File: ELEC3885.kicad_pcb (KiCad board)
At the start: 2 copper layers, 138 x 81.5 mm, 41 parts, among them J1 MicInstIn, J2 LineIn, J3 HeadPhoneOut, J4 LineOutR, J5 LineOutL, J6 Conn_01x24_Female, J7 Conn_01x24_Female, J8 Conn_01x06_Female, J9 Conn_01x05_Female, SW1 SW_Push, SW2 SW_Push, SW3 SW_Push, SW4 SW_Push, U1 AP7313, U2 SGTL5000XNLA3, U3 Teensy4.1

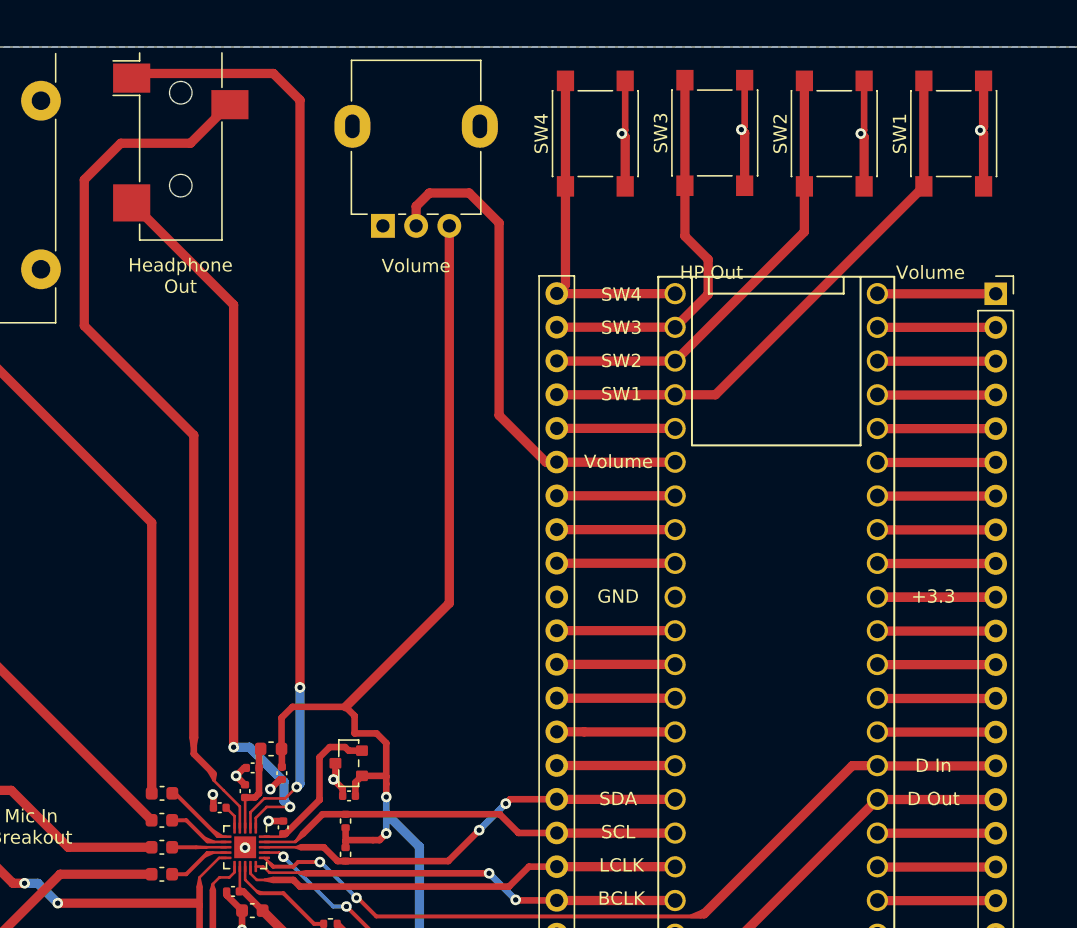
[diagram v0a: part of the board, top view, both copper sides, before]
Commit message: Moved to Rev 3, button + LED ui added
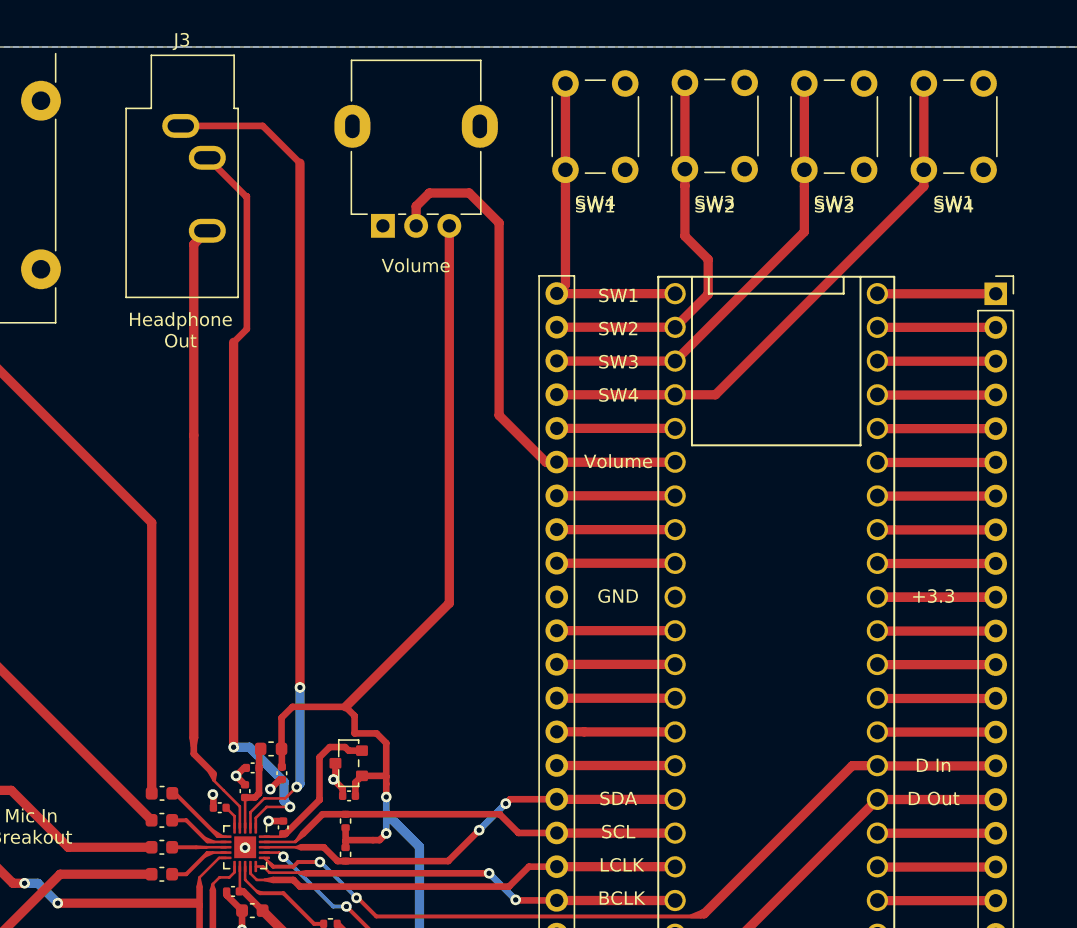
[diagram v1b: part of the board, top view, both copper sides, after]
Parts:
- J3: footprint Connector_Audio:Jack_3.5mm_CUI_SJ-3523-SMT_Horizontal -> Connector_Audio:Jack_3.5mm_CUI_SJ1-3533NG_Horizontal
- SW1, SW2, SW3: footprint Button_Switch_SMD:SW_Push_1P1T_NO_6x6mm_H9.5mm -> Button_Switch_THT:SW_PUSH_6mm
- SW4: footprint Button_Switch_SMD:SW_Push_1P1T_NO_6x6mm_H9.5mm -> Button_Switch_THT:SW_PUSH_6mm_H4.3mm
- moved SW3 3.53 mm to (170.5, 74.2)
- moved SW1 3.53 mm to (188.5, 74.2)
- moved SW2 3.53 mm to (179.5, 74.2)
- moved SW4 3.53 mm to (161.5, 74.2)
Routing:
- net GND: track 46.3 -> 12.6 mm, vias 12 -> 8
- net /Audio/HP_L: track 88.5 -> 68.4 mm
- net /Audio/HP_VGND: track 71.7 -> 62.7 mm
- net /Audio/HP_R: track 54.8 -> 56.7 mm
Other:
- board text removed: "HP Out"

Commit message: Rev3 PCB layout started
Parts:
- removed J8: Conn_01x06_Female, Connector_PinSocket_2.54mm:PinSocket_1x06_P2.54mm_Vertical
- removed MK1: InternalMic, Connector_PinSocket_2.54mm:PinSocket_1x02_P2.54mm_Vertical
- removed SW1, SW2, SW3: SW_Push, Button_Switch_THT:SW_PUSH_6mm
- removed SW4: SW_Push, Button_Switch_THT:SW_PUSH_6mm_H4.3mm
- added C13: 4u7, Capacitor_SMD:C_0402_1005Metric, F.Cu at (250.7, 72.8)
- added C14: 4u7, Capacitor_SMD:C_0402_1005Metric, F.Cu at (249.8, 76.0)
- added C15: 100n, Capacitor_SMD:C_0402_1005Metric, B.Cu at (115.2, 84.5)
- added C16: 6n8, Capacitor_SMD:C_0402_1005Metric, B.Cu at (103.7, 79.4)
- added C17: 6n8, Capacitor_SMD:C_0402_1005Metric, B.Cu at (101.2, 79.4)
- added C18: 8u2, Capacitor_SMD:C_0402_1005Metric, B.Cu at (106.8, 86.4)
- added C19: 22u, Capacitor_SMD:C_0603_1608Metric, F.Cu at (250.1, 78.3)
- added C20: 22u, Capacitor_SMD:C_0603_1608Metric, F.Cu at (252.2, 89.9)
- added D1: LED_RGBK, LED_THT:LED_D5.0mm-4_RGB, F.Cu at (106.0, 140.4)
- added D10: LED, LED_SMD:LED_0201_0603Metric, F.Cu at (258.7, 68.0)
- added D2: LED_RGBK, LED_THT:LED_D5.0mm-4_RGB, F.Cu at (122.8, 140.4)
- added D3: LED_RGBK, LED_THT:LED_D5.0mm-4_RGB, F.Cu at (139.5, 140.4)
- added D4: LED_RGBK, LED_THT:LED_D5.0mm-4_RGB, F.Cu at (156.3, 140.4)
- added D5: LED_RGBK, LED_THT:LED_D5.0mm-4_RGB, F.Cu at (173.0, 140.4)
- added D6: LED_RGBK, LED_THT:LED_D5.0mm-4_RGB, F.Cu at (189.8, 140.4)
- added D7: LED_RGBK, LED_THT:LED_D5.0mm-4_RGB, F.Cu at (206.5, 140.4)
- added D8: LED_RGBK, LED_THT:LED_D5.0mm-4_RGB, F.Cu at (223.3, 140.4)
- added L1: 22uH, Inductor_SMD:L_6.3x6.3_H3, F.Cu at (255.9, 82.9)
- added R10: 100R, Resistor_SMD:R_0402_1005Metric, F.Cu at (198.5, 148.8)
- added R11: 100R, Resistor_SMD:R_0402_1005Metric, F.Cu at (215.2, 148.8)
- added R12: 100R, Resistor_SMD:R_0402_1005Metric, F.Cu at (84.2, 122.6)
- added R13: 100R, Resistor_SMD:R_0402_1005Metric, F.Cu at (82.2, 125.2)
- added R14: 270R, Resistor_SMD:R_0402_1005Metric, F.Cu at (218.2, 140.4)
- added R15: 270R, Resistor_SMD:R_0402_1005Metric, F.Cu at (218.2, 139.1)
- added R16: 270R, Resistor_SMD:R_0402_1005Metric, F.Cu at (218.2, 137.9)
- added R17: 270R, Resistor_SMD:R_0402_1005Metric, F.Cu at (184.7, 140.4)
- added R18: 270R, Resistor_SMD:R_0402_1005Metric, F.Cu at (184.7, 139.1)
- added R19: 270R, Resistor_SMD:R_0402_1005Metric, F.Cu at (184.7, 137.9)
- added R20: 270R, Resistor_SMD:R_0402_1005Metric, F.Cu at (201.4, 140.4)
- added R21: 270R, Resistor_SMD:R_0402_1005Metric, F.Cu at (201.4, 139.1)
- added R22: 270R, Resistor_SMD:R_0402_1005Metric, F.Cu at (151.2, 137.9)
- added R23: 270R, Resistor_SMD:R_0402_1005Metric, F.Cu at (151.2, 140.5)
- added R24: 270R, Resistor_SMD:R_0402_1005Metric, F.Cu at (167.9, 139.1)
- added R25: 270R, Resistor_SMD:R_0402_1005Metric, F.Cu at (201.4, 137.8)
- added R26: 270R, Resistor_SMD:R_0402_1005Metric, F.Cu at (134.4, 140.4)
- added R27: 270R, Resistor_SMD:R_0402_1005Metric, F.Cu at (151.2, 139.2)
- added R28: 270R, Resistor_SMD:R_0402_1005Metric, F.Cu at (167.9, 137.8)
- added R29: 270R, Resistor_SMD:R_0402_1005Metric, F.Cu at (167.9, 140.4)
- added R30: 270R, Resistor_SMD:R_0402_1005Metric, F.Cu at (100.9, 139.1)
- added R31: 270R, Resistor_SMD:R_0402_1005Metric, F.Cu at (117.7, 137.9)
- added R32: 270R, Resistor_SMD:R_0402_1005Metric, F.Cu at (117.7, 140.5)
- added R33: 270R, Resistor_SMD:R_0402_1005Metric, F.Cu at (134.4, 139.1)
- added R34: 270R, Resistor_SMD:R_0402_1005Metric, F.Cu at (100.9, 137.9)
- added R35: 270R, Resistor_SMD:R_0402_1005Metric, F.Cu at (100.9, 140.4)
- added R36: 270R, Resistor_SMD:R_0402_1005Metric, F.Cu at (117.7, 139.2)
- added R37: 270R, Resistor_SMD:R_0402_1005Metric, F.Cu at (134.4, 137.8)
- added R38: 1k, Resistor_SMD:R_0402_1005Metric, B.Cu at (99.2, 79.4)
- added R39: 1k, Resistor_SMD:R_0402_1005Metric, B.Cu at (105.7, 79.4)
- added R4: 2k, Resistor_SMD:R_0402_1005Metric, F.Cu at (247.9, 70.5)
- added R40: 100k, Resistor_SMD:R_0603_1608Metric, B.Cu at (96.8, 85.7)
- added R41: 100k, Resistor_SMD:R_0603_1608Metric, B.Cu at (96.8, 84.0)
- added R42: 9k, Resistor_SMD:R_0603_1608Metric, B.Cu at (99.7, 81.6)
- added R43: 9k, Resistor_SMD:R_0603_1608Metric, B.Cu at (105.0, 81.0)
- added R44: 10k, Resistor_SMD:R_0603_1608Metric, B.Cu at (104.7, 82.6)
- added R45: 10k, Resistor_SMD:R_0603_1608Metric, B.Cu at (105.5, 85.0)
- added R46: 1k, Resistor_SMD:R_0402_1005Metric, B.Cu at (106.8, 87.8)
- added R47: 100R, Resistor_SMD:R_0402_1005Metric, B.Cu at (108.9, 86.4)
- added R48: R, Resistor_SMD:R_0402_1005Metric, F.Cu at (251.9, 70.6)
- added R49: 15k, Resistor_SMD:R_0603_1608Metric, F.Cu at (251.4, 86.0)
- added R5: 100R, Resistor_SMD:R_0402_1005Metric, F.Cu at (114.7, 148.8)
- added R50: 2k, Resistor_SMD:R_0402_1005Metric, F.Cu at (250.0, 85.6)
- added R6: 100R, Resistor_SMD:R_0402_1005Metric, F.Cu at (131.5, 148.8)
- added R7: 100R, Resistor_SMD:R_0402_1005Metric, F.Cu at (148.2, 148.8)
- added R8: 100R, Resistor_SMD:R_0402_1005Metric, F.Cu at (165.2, 148.8)
- added R9: 100R, Resistor_SMD:R_0402_1005Metric, F.Cu at (181.7, 148.8)
- added SW10: SW_Push, Button_Switch_SMD:SW_Push_1P1T_NO_6x6mm_H9.5mm, F.Cu at (189.8, 149.8)
- added SW11: SW_Push, Button_Switch_SMD:SW_Push_1P1T_NO_6x6mm_H9.5mm, F.Cu at (206.5, 149.8)
- added SW12: SW_Push, Button_Switch_SMD:SW_Push_1P1T_NO_6x6mm_H9.5mm, F.Cu at (223.2, 149.8)
- added SW5: SW_Push, Button_Switch_SMD:SW_Push_1P1T_NO_6x6mm_H9.5mm, F.Cu at (106.0, 149.8)
- added SW6: SW_Push, Button_Switch_SMD:SW_Push_1P1T_NO_6x6mm_H9.5mm, F.Cu at (122.8, 149.8)
- added SW7: SW_Push, Button_Switch_SMD:SW_Push_1P1T_NO_6x6mm_H9.5mm, F.Cu at (139.5, 149.8)
- added SW8: SW_Push, Button_Switch_SMD:SW_Push_1P1T_NO_6x6mm_H9.5mm, F.Cu at (156.3, 149.8)
- added SW9: SW_Push, Button_Switch_SMD:SW_Push_1P1T_NO_6x6mm_H9.5mm, F.Cu at (173.0, 149.8)
- added TP1: TP_RCLK, TestPoint:TestPoint_Pad_D1.0mm, F.Cu at (14.9, 83.5)
- added TP2: TP_SRCLK_N, TestPoint:TestPoint_Pad_D1.0mm, F.Cu at (14.9, 86.6)
- added TP3: TP_SRCLK, TestPoint:TestPoint_Pad_D1.0mm, F.Cu at (14.9, 89.7)
- added TP4: TP_DS, TestPoint:TestPoint_Pad_D1.0mm, F.Cu at (14.9, 92.7)
- added TP5: TP_BUTTON_ARRAY, TestPoint:TestPoint_Pad_D1.0mm, F.Cu at (14.9, 95.8)
- added U10: MT3608, Package_TO_SOT_SMD:SOT-23-6, F.Cu at (250.3, 81.2)
- added U11: L7805, Package_TO_SOT_SMD:TO-252-2, F.Cu at (254.4, 94.8)
- added U4: 74HC595, Package_SO:SOP-16_4.4x10.4mm_P1.27mm, F.Cu at (155.0, 128.9)
- added U5: 74HC595, Package_SO:SOP-16_4.4x10.4mm_P1.27mm, F.Cu at (187.8, 128.9)
- added U6: 74HC595, Package_SO:SOP-16_4.4x10.4mm_P1.27mm, F.Cu at (105.2, 128.9)
- added U7: LCD_Conn, Connector_PinHeader_2.54mm:PinHeader_1x08_P2.54mm_Vertical, F.Cu at (-20.8, 114.4)
- added U8: NE5532, Package_SO:SOIC-8-1EP_3.9x4.9mm_P1.27mm_EP2.29x3mm, B.Cu at (110.8, 83.1)
- added U9: MCP73831-2-OT, Package_TO_SOT_SMD:SOT-23-5, F.Cu at (248.3, 73.4)
- C1, C10, C11, C12, C13, C14, C2, C3, C4, C5, C6, C7, C9, J1, J2, J4, J5, R1, R2, R3, R4, U1, U2, U3: moved to B.Cu
- C8: value .1uF -> 0.1uF; moved to B.Cu
- FB1: value FerriteBead -> 600; moved to B.Cu
- J3: footprint Connector_Audio:Jack_3.5mm_CUI_SJ1-3533NG_Horizontal -> Connector_Audio:Jack_3.5mm_CUI_SJ-3523-SMT_Horizontal; moved to B.Cu
- J6: value Conn_01x24_Female -> Conn_LiPo; footprint Connector_PinSocket_2.54mm:PinSocket_1x24_P2.54mm_Vertical -> Connector_JST:JST_EH_S2B-EH_1x02_P2.50mm_Horizontal; moved to B.Cu
- J7: value Conn_01x24_Female -> USB_B_Micro; footprint Connector_PinSocket_2.54mm:PinSocket_1x24_P2.54mm_Vertical -> Connector_USB:USB_Micro-B_Amphenol_10103594-0001LF_Horizontal; moved to B.Cu
- moved C14 253.2 mm to (376.8, 64.3), turned to 0 degrees
- moved R4 251.0 mm to (376.8, 66.1), turned to 0 degrees
- moved C13 246.3 mm to (376.3, 69.4), turned to -90 degrees
- moved C5 244.7 mm to (366.6, 61.0), turned to -90 degrees
- moved C4 242.2 mm to (364.6, 61.0), turned to -90 degrees
- moved C12 239.7 mm to (362.5, 61.0), turned to 90 degrees
- moved C2 239.7 mm to (367.9, 66.3), turned to 90 degrees
- moved C1 239.7 mm to (369.4, 67.8), turned to 90 degrees
- moved C11 237.2 mm to (360.5, 61.0), turned to 90 degrees
- moved U2 234.5 mm to (364.6, 67.3), turned to 0 degrees
- moved R1 233.7 mm to (370.4, 73.7), turned to 90 degrees
- moved C6 233.2 mm to (361.6, 65.3), turned to -90 degrees
- moved C9 229.4 mm to (360.4, 67.3), turned to 180 degrees
- moved C8 229.2 mm to (363.1, 70.1), turned to 180 degrees
- moved C10 226.6 mm to (358.6, 67.8), turned to 90 degrees
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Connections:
- J1 pad 3: GND -> /Audio/MIC_VGND
- J6 pad 1: Net-(J6-Pad1) -> Net-(J6-Pin_1)
- J6 pad 2: Net-(J6-Pad2) -> GND
- J7 pad 1: Net-(J7-Pad1) -> Net-(D9-K)
- J7 pad 2: GND -> unconnected-(J7-D--Pad2)
- J7 pad 3: +3.3V -> unconnected-(J7-D+-Pad3)
- J7 pad 4: /Audio/MCLK -> unconnected-(J7-ID-Pad4)
- J7 pad 5: Net-(J7-Pad5) -> GND
- J7 pad 6: /Audio/BCLK -> GND
- U3 pad 11: Net-(J6-Pad14) -> /Teensy/LCD_DC
- U3 pad 12: Net-(J6-Pad13) -> /Teensy/LCD_CS
- U3 pad 13: Net-(J6-Pad12) -> /Teensy/LCD_MOSI
- U3 pad 14: Net-(J6-Pad11) -> /Teensy/LCD_MISO
- U3 pad 16: Net-(J6-Pad9) -> unconnected-(U3-24_A10_TX6_SCL2-Pad16)
- U3 pad 17: Net-(J6-Pad8) -> unconnected-(U3-25_A11_RX6_SDA2-Pad17)
- U3 pad 18: Net-(J6-Pad7) -> unconnected-(U3-26_A12_MOSI1-Pad18)
- U3 pad 19: Net-(J6-Pad6) -> unconnected-(U3-27_A13_SCK1-Pad19)
- U3 pad 2: Net-(J6-Pad23) -> unconnected-(U3-0_RX1_CRX2_CS1-Pad2)
- U3 pad 20: Net-(J6-Pad5) -> unconnected-(U3-28_RX7-Pad20)
- U3 pad 21: Net-(J6-Pad4) -> unconnected-(U3-29_TX7-Pad21)
- U3 pad 22: Net-(J6-Pad3) -> unconnected-(U3-30_CRX3-Pad22)
- U3 pad 23: Net-(J6-Pad2) -> unconnected-(U3-31_CTX3-Pad23)
- U3 pad 24: Net-(J6-Pad1) -> unconnected-(U3-32_OUT1B-Pad24)
- U3 pad 25: /Teensy/BUTTON_3 -> unconnected-(U3-33_MCLK2-Pad25)
- U3 pad 26: /Teensy/BUTTON_2 -> unconnected-(U3-34_RX8-Pad26)
- U3 pad 27: /Teensy/BUTTON_1 -> unconnected-(U3-35_TX8-Pad27)
- U3 pad 28: /Teensy/BUTTON_0 -> unconnected-(U3-36_CS-Pad28)
- U3 pad 29: Net-(J7-Pad20) -> unconnected-(U3-37_CS-Pad29)
- U3 pad 3: Net-(J6-Pad22) -> unconnected-(U3-1_TX1_CTX2_MISO1-Pad3)
- U3 pad 31: Net-(J7-Pad18) -> unconnected-(U3-39_MISO1_OUT1A-Pad31)
- U3 pad 32: Net-(J7-Pad17) -> unconnected-(U3-40_A16-Pad32)
- U3 pad 33: Net-(J7-Pad16) -> /Teensy/BUTTON_ARRAY
- U3 pad 35: Net-(J7-Pad14) -> /Teensy/LCD_CLK
- U3 pad 36: Net-(J7-Pad13) -> unconnected-(U3-14_A0_TX3_SPDIF_OUT-Pad36)
- U3 pad 37: Net-(J7-Pad12) -> unconnected-(U3-15_A1_RX3_SPDIF_IN-Pad37)
- U3 pad 38: Net-(J7-Pad11) -> unconnected-(U3-16_A2_RX4_SCL1-Pad38)
- U3 pad 39: Net-(J7-Pad10) -> unconnected-(U3-17_A3_TX4_SDA1-Pad39)
- U3 pad 4: Net-(J6-Pad21) -> unconnected-(U3-2_OUT2-Pad4)
- U3 pad 44: Net-(J7-Pad5) -> unconnected-(U3-22_A8_CTX1-Pad44)
- U3 pad 48: Net-(J7-Pad1) -> unconnected-(U3-VIN-Pad48)
- U3 pad 5: Net-(J6-Pad20) -> unconnected-(U3-3_LRCLK2-Pad5)
- U3 pad 6: Net-(J6-Pad19) -> unconnected-(U3-4_BCLK2-Pad6)
- U3 pad 7: Net-(J6-Pad18) -> unconnected-(U3-5_IN2-Pad7)
- U3 pad 8: Net-(J6-Pad17) -> unconnected-(U3-6_OUT1D-Pad8)
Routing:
- net +3.3V: track 223.5 -> 82.7 mm, vias 4 -> 3
- net /Teensy/BUTTON_ARRAY: track 0.00 -> 128.6 mm
- net /UI/LED_SRCLK: track 0.00 -> 91.7 mm
- net /UI/LED_RCLK: track 0.00 -> 89.8 mm, vias 0 -> 4
- net Net-(U4-~{OE}): track 0.00 -> 87.5 mm, vias 0 -> 4
- net /Audio/LINE_OUT_R: track 78.4 -> 0.00 mm
- net /Audio/LINE_IN_R: track 67.8 -> 0.00 mm
- net /Audio/HP_L: track 68.4 -> 8.27 mm
- net Net-(U4-QH'): track 0.00 -> 59.1 mm, vias 0 -> 2
- net /Audio/LINE_IN_L: track 54.2 -> 0.00 mm
- net /Audio/LINE_OUT_L: track 51.7 -> 0.00 mm
- net /Audio/D_IN: track 62.0 -> 10.6 mm
- net /Audio/D_OUT: track 62.5 -> 12.3 mm
- net /Audio/HP_VGND: track 62.7 -> 13.1 mm
- net /Audio/HP_R: track 56.7 -> 10.6 mm
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- added copper zone on In1.Cu, net GND
- removed copper zone on B.Cu, net GND
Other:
- board size 138 x 81.5 mm -> 175 x 102 mm
- copper layers 2 -> 4
- board text removed: "+"
- board text removed: "+3.3"
- board text removed: "-"
- board text removed: "BCLK"
- board text removed: "D In"
- board text removed: "D Out"
- board text removed: "ECM"
- board text removed: "Headphone Out"
- board text removed: "In"
- board text removed: "LCLK"
- board text removed: "Line In"
- board text removed: "Line Out L"
- board text removed: "Line Out R"
- board text removed: "MCLK"
- board text removed: "Mic In"
- board text removed: "Mic In Breakout"
- board text removed: "SCL"
- board text removed: "SDA"
- board text removed: "SW1"
- board text removed: "SW2"
- board text removed: "SW3"
- board text removed: "SW4"
- board text removed: "Volume"

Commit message: Rev3 rework, diff amp jumpers added
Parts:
- removed the C13 at (376.3, 69.4)
- removed the C14 at (376.8, 64.3)
- removed the R4 at (376.8, 66.1)
- added D11: SS34, Diode_SMD:D_SMC, F.Cu at (230.8, 66.0)
- added D9: uClamp0571P, Luke_library:DFN1610-2, F.Cu at (235.1, 40.4)
- added JP1: JP1, Jumper:SolderJumper-3_P1.3mm_Open_RoundedPad1.0x1.5mm, B.Cu at (85.1, 43.5)
- added JP2: JP2, Jumper:SolderJumper-3_P1.3mm_Open_RoundedPad1.0x1.5mm, B.Cu at (75.3, 43.5)
- added JP3: JP3, Jumper:SolderJumper-3_P1.3mm_Open_RoundedPad1.0x1.5mm, B.Cu at (80.2, 43.5)
- added RV2: 10k, Potentiometer_THT:Potentiometer_Alpha_RD901F-40-00D_Single_Vertical, F.Cu at (166.1, 69.1)
- added RV3: 10k, Potentiometer_THT:Potentiometer_Alpha_RD901F-40-00D_Single_Vertical, F.Cu at (188.0, 69.1)
- added RV4: 10k, Potentiometer_THT:Potentiometer_Alpha_RD901F-40-00D_Single_Vertical, F.Cu at (209.9, 69.1)
- added SW1: SW_SPST, Button_Switch_THT:SW_CuK_OS102011MA1QN1_SPDT_Angled, F.Cu at (239.6, 52.5)
- U7: footprint Connector_PinHeader_2.54mm:PinHeader_1x08_P2.54mm_Vertical -> Luke_library:Adafruit_3.5_TFT_SPI
- moved C5 241.4 mm to (126.3, 83.1), turned to 0 degrees
- moved C4 239.5 mm to (126.3, 85.1), turned to 0 degrees
- moved C12 237.7 mm to (126.3, 87.2), turned to 180 degrees
- moved C2 236.8 mm to (131.6, 81.8), turned to 180 degrees
- moved C1 236.6 mm to (133.1, 80.4), turned to 180 degrees
- moved C11 235.9 mm to (126.3, 89.2), turned to 180 degrees
- moved U2 232.7 mm to (132.5, 85.1), turned to 90 degrees
- moved C6 232.1 mm to (130.6, 88.1), turned to 0 degrees
- moved R1 231.5 mm to (139.0, 79.4), turned to 180 degrees
- moved C9 228.9 mm to (132.5, 89.4), turned to -90 degrees
- moved C8 228.3 mm to (135.4, 86.6), turned to -90 degrees
- moved C10 226.7 mm to (133.1, 91.1), turned to 180 degrees
- moved R3 225.2 mm to (140.1, 84.6), turned to -90 degrees
- moved C7 224.7 mm to (135.3, 90.7), turned to 90 degrees
- moved FB1 223.9 mm to (134.5, 92.5), turned to 180 degrees
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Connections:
- C19 pad 1: Net-(J6-Pin_1) -> Net-(SW1-B)
- J1 pad 1: Net-(J1-Pad1) -> Net-(JP1-C)
- J1 pad 2: Net-(J1-Pad2) -> Net-(JP2-C)
- J1 pad 3: /Audio/MIC_VGND -> Net-(JP3-C)
- L1 pad 1: Net-(J6-Pin_1) -> Net-(SW1-B)
- R17 pad 2: Net-(D6-RA) -> Net-(D7-RA)
- R18 pad 2: Net-(D6-GA) -> Net-(D7-GA)
- R19 pad 2: Net-(D6-BA) -> Net-(D7-BA)
- R20 pad 2: Net-(D7-RA) -> Net-(D6-RA)
- R21 pad 2: Net-(D7-GA) -> Net-(D6-GA)
- R25 pad 2: Net-(D7-BA) -> Net-(D6-BA)
- R38 pad 1: Net-(J1-Pad2) -> Net-(JP2-B)
- R39 pad 1: Net-(J1-Pad1) -> Net-(JP1-A)
- TP1 pad 1: /UI/LED_RCLK -> /Teensy/LED_RCLK
- TP3 pad 1: /UI/LED_SRCLK -> /Teensy/LED_SRCLK
- TP4 pad 1: /UI/LED_DS -> /Teensy/LED_DS
- U10 pad 4: Net-(J6-Pin_1) -> Net-(SW1-B)
- U10 pad 5: Net-(J6-Pin_1) -> Net-(SW1-B)
- U3 pad 16: unconnected-(U3-24_A10_TX6_SCL2-Pad16) -> /Teensy/UI_POT1
- U3 pad 17: unconnected-(U3-25_A11_RX6_SDA2-Pad17) -> /Teensy/UI_POT2
- U3 pad 18: unconnected-(U3-26_A12_MOSI1-Pad18) -> /Teensy/UI_POT3
- U3 pad 19: unconnected-(U3-27_A13_SCK1-Pad19) -> /Audio/VOLUME_CONTROL
- U3 pad 30: /Audio/VOLUME_CONTROL -> unconnected-(U3-38_CS1_IN1-Pad30)
- U3 pad 37: unconnected-(U3-15_A1_RX3_SPDIF_IN-Pad37) -> /Teensy/LED_SRCLK
- U3 pad 38: unconnected-(U3-16_A2_RX4_SCL1-Pad38) -> /Teensy/LED_RCLK
- U3 pad 39: unconnected-(U3-17_A3_TX4_SDA1-Pad39) -> /Teensy/LED_DS
- U3 pad 48: unconnected-(U3-VIN-Pad48) -> +5V
- U4 pad 11: /UI/LED_SRCLK -> /Teensy/LED_SRCLK
- U4 pad 12: /UI/LED_RCLK -> /Teensy/LED_RCLK
- U5 pad 11: /UI/LED_SRCLK -> /Teensy/LED_SRCLK
- U5 pad 12: /UI/LED_RCLK -> /Teensy/LED_RCLK
- U5 pad 14: /UI/LED_DS -> /Teensy/LED_DS
- U6 pad 11: /UI/LED_SRCLK -> /Teensy/LED_SRCLK
- U6 pad 12: /UI/LED_RCLK -> /Teensy/LED_RCLK
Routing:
- net +5V: track 1.94 -> 235.8 mm, vias 0 -> 6
- net /Teensy/BUTTON_ARRAY: track 128.6 -> 0.00 mm
- net /Audio/HP_L: track 8.27 -> 130.2 mm, vias 0 -> 2
- net /Teensy/LED_SRCLK: track 0.00 -> 118.2 mm, vias 0 -> 2
- net /Audio/LINE_OUT_R: track 0.00 -> 114.0 mm, vias 0 -> 2
- net /Teensy/LED_RCLK: track 0.00 -> 112.8 mm, vias 0 -> 8
- net +3.3V: track 82.7 -> 192.8 mm, vias 3 -> 7
- net /Audio/HP_VGND: track 13.1 -> 121.6 mm, vias 2 -> 0
- net /Audio/MEMS_IN: track 0.00 -> 105.2 mm, vias 0 -> 3
- net /Audio/HP_R: track 10.6 -> 115.5 mm, vias 2 -> 0
- net /Audio/LINE_OUT_L: track 0.00 -> 94.3 mm, vias 0 -> 2
- net /UI/LED_SRCLK: track 91.7 -> 0.00 mm
- net /UI/LED_RCLK: track 89.8 -> 0.00 mm, vias 4 -> 0
- net /Audio/LINE_IN_R: track 0.00 -> 79.3 mm
- net /Audio/MIC_IN: track 12.5 -> 85.2 mm, vias 0 -> 4
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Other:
- board size 175 x 102 mm -> 190 x 130 mm
- board text added: "DA"
- board text added: "HEADPHONE"
- board text added: "INTERNAL MIC"
- board text added: "LCD"
- board text added: "LINE IN"
- board text added: "LINE OUT"
- board text added: "MIC IN"
- board text added: "N"
- board text added: "SD CARD SLOT"
- board text added: "USB PWR"
- board text removed: "+3.3V"
- board text removed: "GND"
- board text removed: "MEMS Breakout"
- board text removed: "MEMS In"

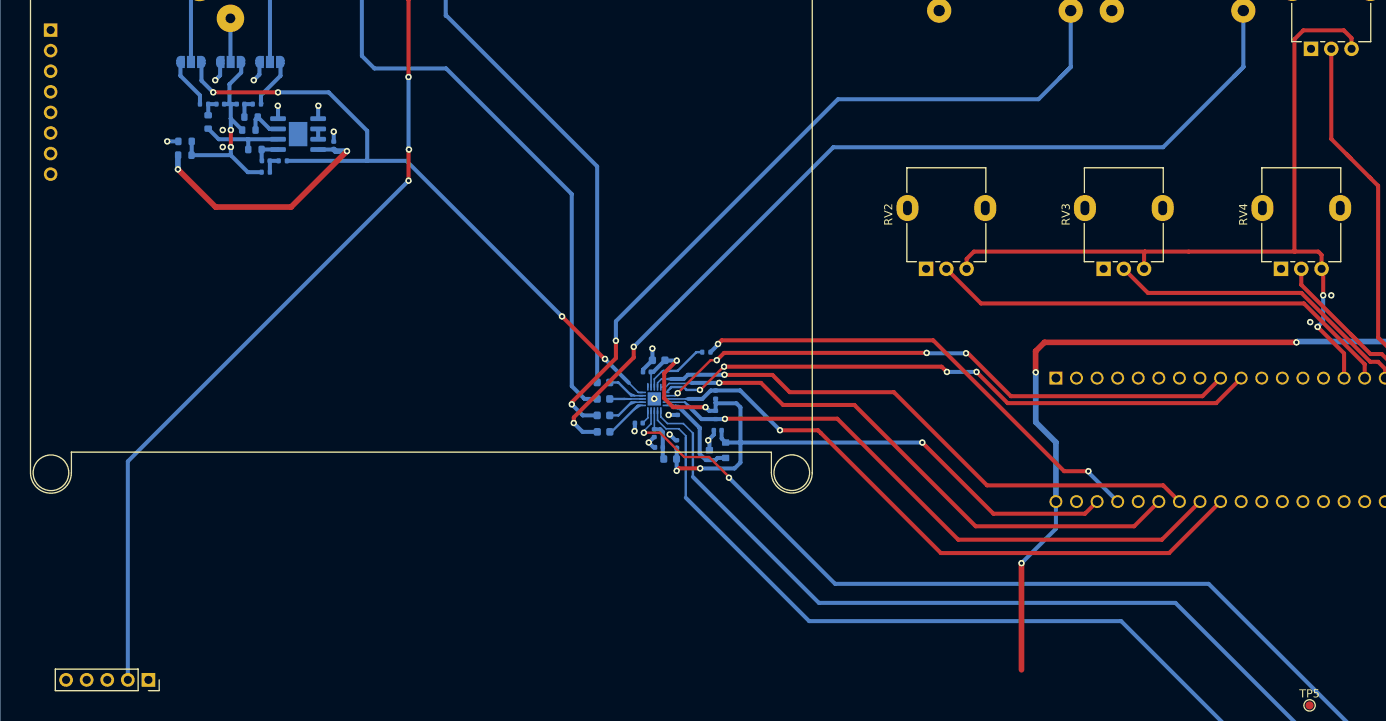
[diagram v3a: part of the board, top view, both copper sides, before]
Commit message: LCD footprint fix
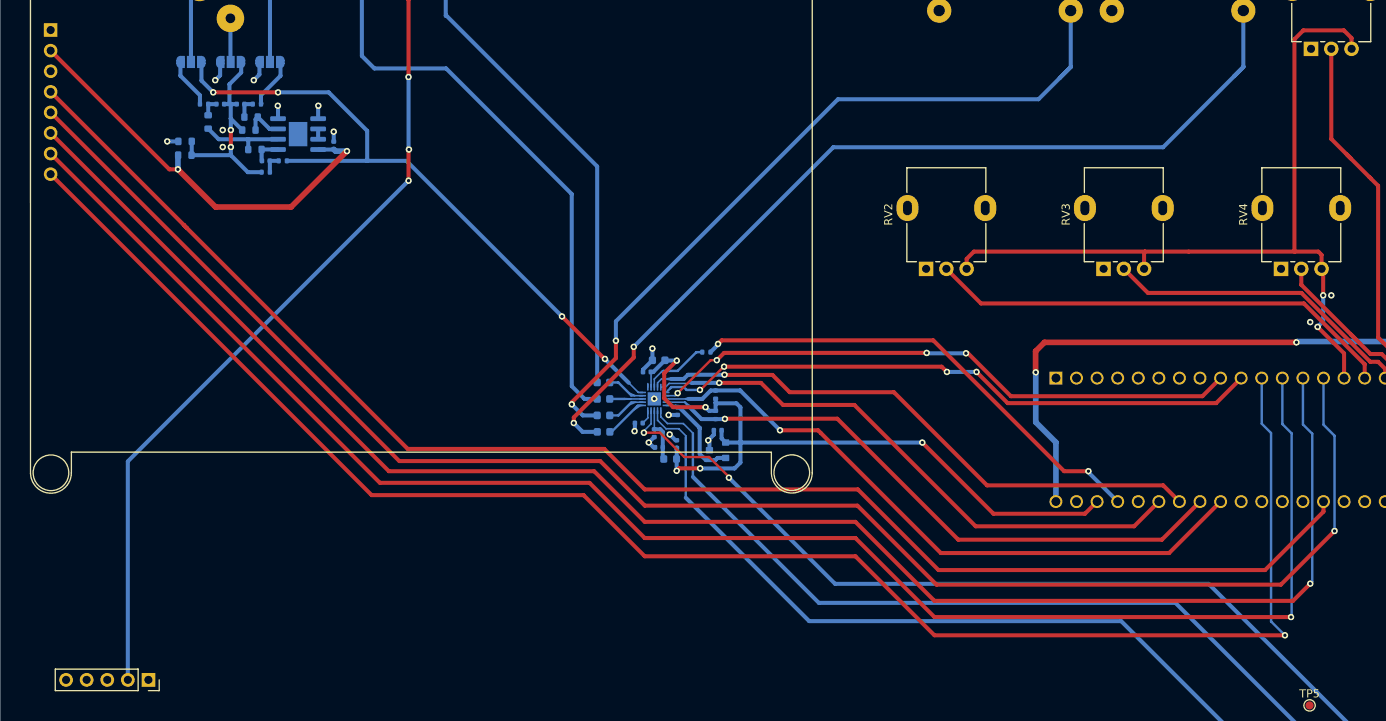
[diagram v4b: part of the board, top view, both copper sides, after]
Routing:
- net /Teensy/LCD_DC: track 0.00 -> 208.8 mm, vias 0 -> 1
- net /Teensy/LCD_CS: track 0.00 -> 206.8 mm, vias 0 -> 1
- net /Teensy/LCD_MOSI: track 0.00 -> 206.2 mm, vias 0 -> 1
- net /Teensy/LCD_MISO: track 0.00 -> 204.9 mm, vias 0 -> 1
- net /Teensy/LCD_CLK: track 0.00 -> 186.3 mm
- net +5V: track 235.8 -> 235.1 mm, vias 6 -> 5
